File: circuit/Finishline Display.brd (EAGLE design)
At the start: 81.3 x 100 mm, 25 parts, among them U1 PCA9501, U2 HEF4066BT, U3 TM1637

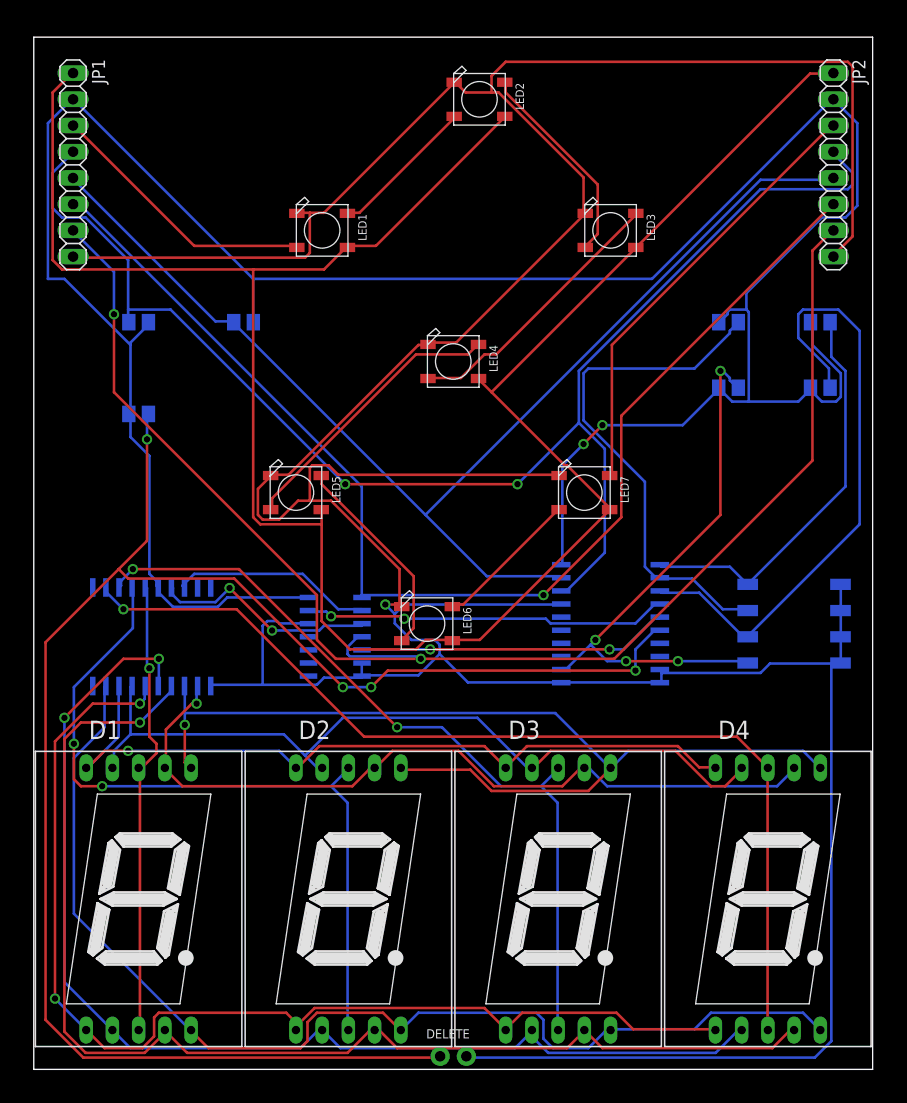
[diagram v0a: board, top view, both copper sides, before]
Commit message: changes circuit to include capacitors
This change adds resistors and capacitors to the LED driver chip
as well as individual caps to each WS2812 LED.
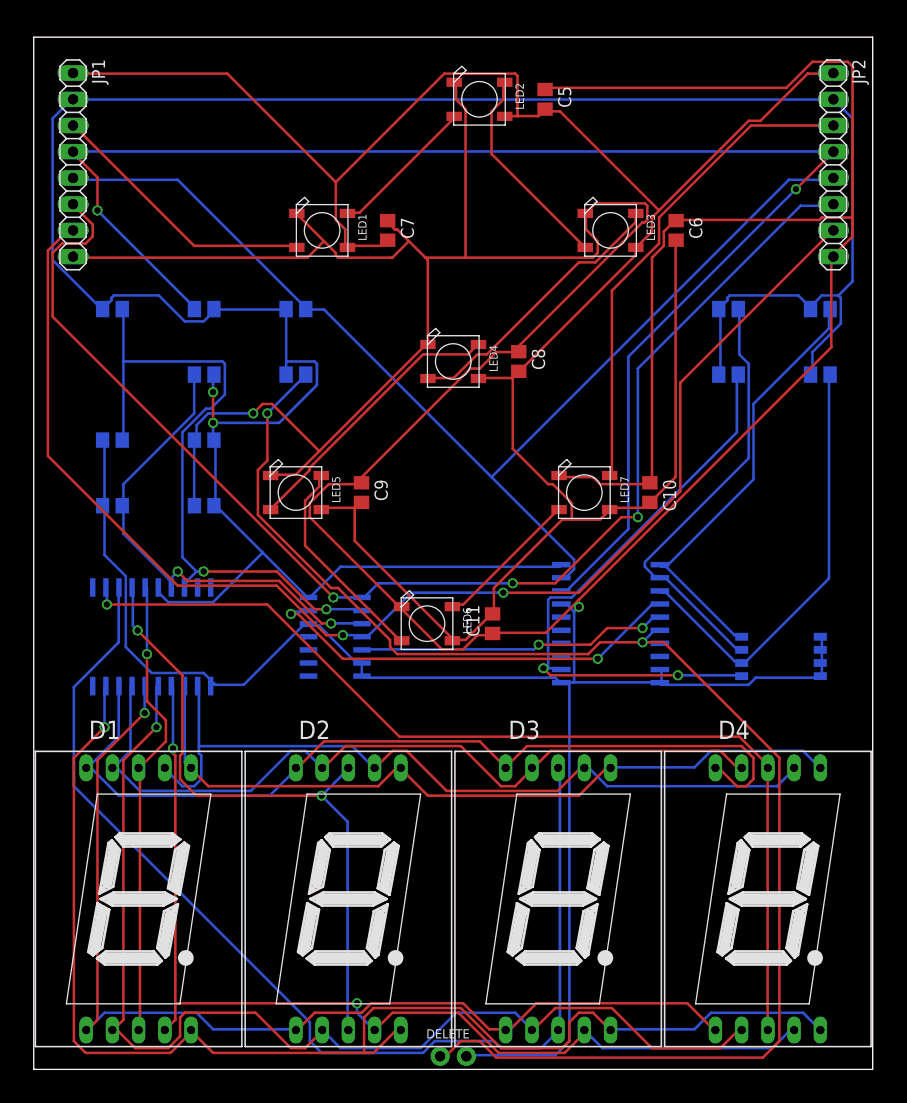
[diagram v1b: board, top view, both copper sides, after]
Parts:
- removed S1: SWS004, smd-special:SMS-004
- added C1, C2: 1nF, rcl:C0805
- added C10, C11, C4, C5, C6, C7, C8, C9: 100nF, rcl:C0805
- added C3: 10nF, rcl:C0805
- added R10, R9: 10K, resistor:M0805
- added SW1: 416131160804, Wurth_Elektronik_Electromechanic_Switchs_rev15b:416131160804
- moved R7 15.7 mm to (25.4, 67.3)
- moved R5 6.48 mm to (16.5, 73.7)
- moved R6 5.24 mm to (25.4, 73.7), turned to 180 degrees
- moved R1 1.27 mm to (76.2, 73.7)
- moved R2 1.27 mm to (67.3, 73.7)
- moved R3 1.27 mm to (76.2, 67.3)
- moved R4 1.27 mm to (67.3, 67.3)
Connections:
- net +5V: now also C10.2, C11.2, C5.2, C6.2, C7.2, C8.2, C9.2
- net 0V: now also C1.1, C10.1, C11.1, C2.1, C3.2, C4.2, C5.1, C6.1, C7.1, C8.1, C9.1, SW1.1, SW1.2, SW1.3, SW1.4; no longer S1.1, S1.2, S1.3, S1.4
- net 3.3V: now also C3.1, C4.1, R10.2, R9.2
- net N$14: now also SW1.8; no longer S1.8
- net N$15: now also SW1.7; no longer S1.7
- net N$16: now also SW1.6; no longer S1.6
- net N$17: now also SW1.5; no longer S1.5
- net N$18: now also C1.2, R9.1
- net N$19: now also C2.2, R10.1
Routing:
- net 0V: track 402.7 -> 526.9 mm, vias 1 -> 2
- net N$18: track 19.7 -> 65.3 mm, vias 0 -> 2
- net N$11: track 77.4 -> 106.9 mm, vias 2 -> 0
- net N$19: track 22.1 -> 46.6 mm
- net N$20: track 163.3 -> 141.5 mm, vias 4 -> 2
- net SEG2: track 95.6 -> 74.4 mm, vias 1 -> 0
- net SEG3: track 118.5 -> 100.5 mm, vias 1 -> 2
- net N$16: track 59.9 -> 42.5 mm
- net SEG8: track 109.5 -> 124.8 mm, vias 0 -> 1
- net +5V: track 209.8 -> 224.9 mm
- net SEG7: track 75.1 -> 86.6 mm, vias 1 -> 0
- net N$10: track 72.9 -> 62.6 mm
- net SCL: track 137.2 -> 147.5 mm
- net DIO: track 139.1 -> 129.0 mm
- net CLK: track 117.5 -> 125.7 mm, vias 1 -> 3
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
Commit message: add Controller brd+sch, fix Display LDR line
An additional board for the controller was added as a Due shield.
The LDR was hooked up to a digital pin, has been changed to use
a separate line which gets patched through the 4066.
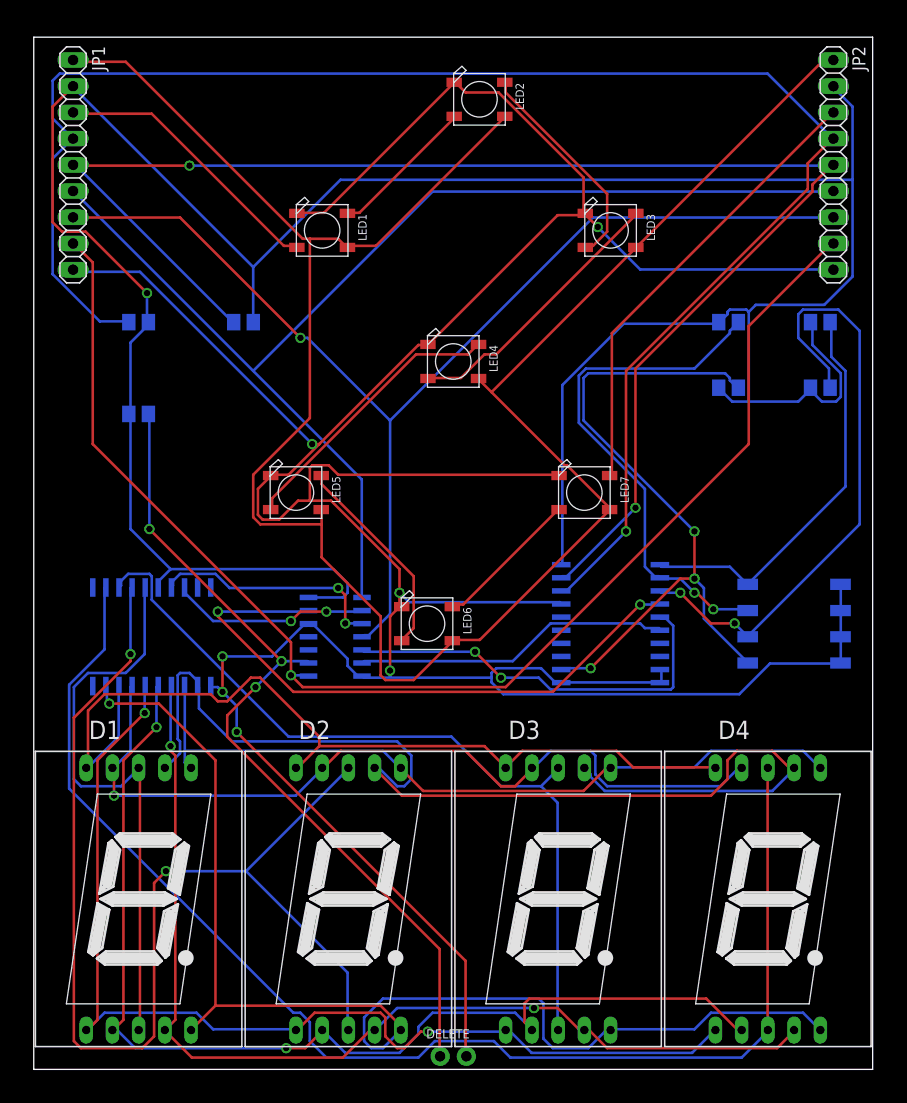
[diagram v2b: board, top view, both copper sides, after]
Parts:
- removed C1, C2: 1nF, rcl:C0805
- removed C10, C11, C4, C5, C6, C7, C8, C9: 100nF, rcl:C0805
- removed C3: 10nF, rcl:C0805
- removed R10, R9: 10K, resistor:M0805
- removed SW1: 416131160804, Wurth_Elektronik_Electromechanic_Switchs_rev15b:416131160804
- added S1: SWS004, smd-special:SMS-004
- JP1, JP2: device pinhead:1X08 -> pinhead:1X09
- moved R7 15.7 mm to (10.2, 63.5)
- moved R5 6.48 mm to (10.2, 72.4)
- moved R6 5.24 mm to (20.3, 72.4), turned to 0 degrees
- moved R1 1.27 mm to (76.2, 72.4)
- moved R2 1.27 mm to (67.3, 72.4)
- moved R3 1.27 mm to (76.2, 66.0)
- moved R4 1.27 mm to (67.3, 66.0)
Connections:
- removed net 0V: C1.1, C10.1, C11.1, C2.1, C3.2, C4.2, C5.1, C6.1, C7.1, C8.1, C9.1, JP1.8, JP2.8, LED1.3-GND, LED2.3-GND, LED3.3-GND, LED4.3-GND, LED5.3-GND, LED6.3-GND, LED7.3-GND, R8.2, SW1.1, SW1.2, SW1.3, SW1.4, U1.10, U1.11, U1.17, U1.9, U2.12, U2.6, U2.7, U3.1
- new net GND: JP1.9, JP2.9, LED1.3-GND, LED2.3-GND, LED3.3-GND, LED4.3-GND, LED5.3-GND, LED6.3-GND, LED7.3-GND, R8.2, S1.1, S1.2, S1.3, S1.4, U1.10, U1.11, U1.17, U1.9, U2.12, U2.7, U3.1
- new net LDR: JP1.8, JP2.8, U2.8
- new net N$23: U1.6, U2.6
- net +5V: no longer C10.2, C11.2, C5.2, C6.2, C7.2, C8.2, C9.2
- net 3.3V: no longer C3.1, C4.1, R10.2, R9.2
- net N$14: now also S1.8; no longer SW1.8
- net N$15: now also S1.7; no longer SW1.7
- net N$16: now also S1.6; no longer SW1.6
- net N$17: now also S1.5; no longer SW1.5
- net N$18: no longer C1.2, R9.1
- net N$19: no longer C2.2, R10.1
- net N$20: now also U2.9; no longer U1.6
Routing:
- net 0V: track 526.9 -> 0.00 mm, vias 2 -> 0
- net GND: track 0.00 -> 358.2 mm, vias 0 -> 7
- net LDR: track 0.00 -> 129.9 mm, vias 0 -> 1
- net N$20: track 141.5 -> 81.0 mm, vias 2 -> 3
- net N$10: track 62.6 -> 112.7 mm
- net N$18: track 65.3 -> 19.3 mm
- net SDA: track 111.6 -> 147.0 mm, vias 0 -> 2
- net SEG1: track 77.1 -> 111.8 mm
- net N$23: track 0.00 -> 30.8 mm
- net N$12: track 98.1 -> 128.4 mm, vias 1 -> 0
- net N$11: track 106.9 -> 78.3 mm
- net N$19: track 46.6 -> 22.9 mm
- net +5V: track 224.9 -> 203.1 mm
- net 3.3V: track 253.9 -> 272.3 mm, vias 2 -> 1
- net N$16: track 42.5 -> 59.9 mm, vias 0 -> 2
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
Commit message: add mounting holes to the Finishline Display board
New PDFs have been added for the display.
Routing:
- net 3.3V: track 272.3 -> 218.0 mm, vias 1 -> 4
- net N$10: track 112.7 -> 68.9 mm
- net SEG1: track 111.8 -> 77.8 mm, vias 0 -> 3
- net N$12: track 128.4 -> 98.3 mm, vias 0 -> 1
- net N$17: track 66.6 -> 90.0 mm, vias 3 -> 5
- net SCL: track 163.3 -> 178.9 mm
- net N$1: track 58.7 -> 44.5 mm
- net N$9: track 56.4 -> 43.5 mm, vias 0 -> 2
- net LDR: track 129.9 -> 142.5 mm
- net N$15: track 50.6 -> 39.2 mm, vias 2 -> 0
- net SEG7: track 86.3 -> 76.3 mm
- net N$13: track 39.4 -> 30.2 mm, vias 2 -> 0
- net +5V: track 203.1 -> 196.6 mm, vias 0 -> 2
- net DIO: track 112.3 -> 118.6 mm, vias 1 -> 3
- net CLK: track 114.4 -> 108.5 mm
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
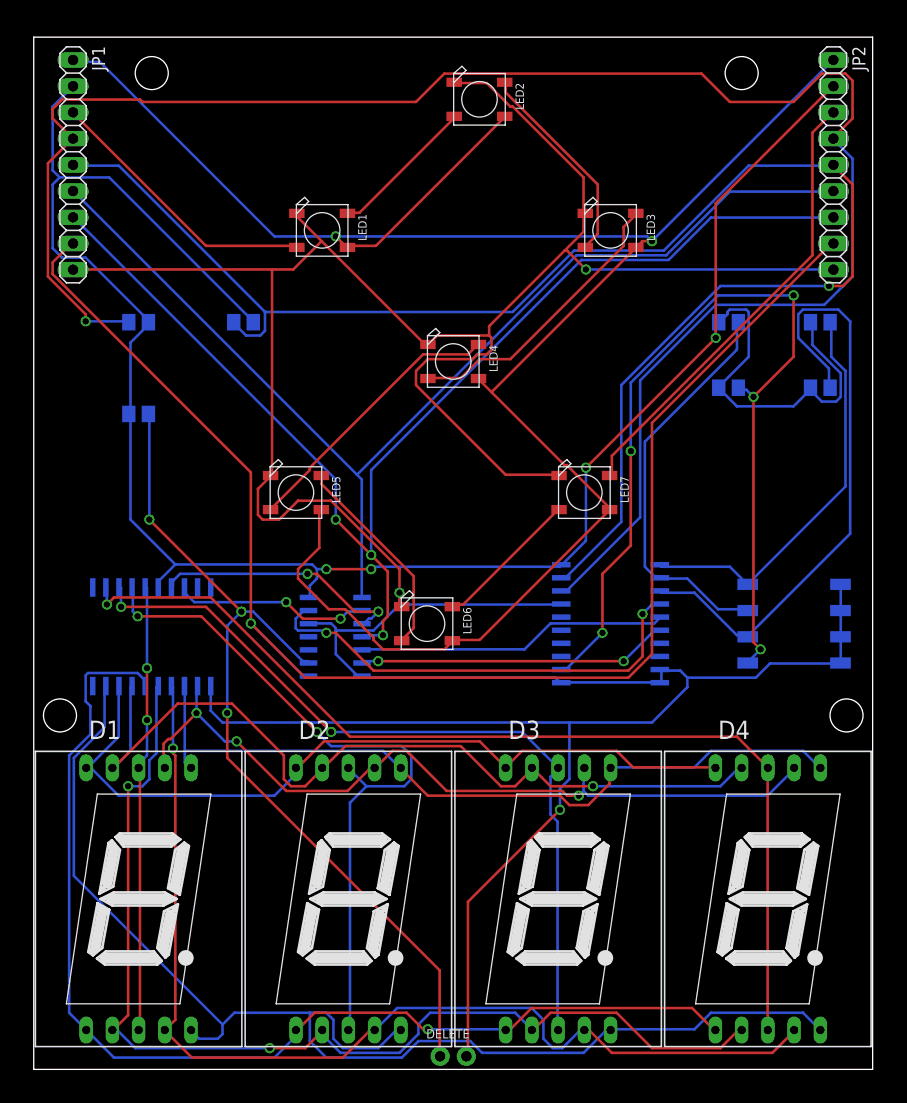
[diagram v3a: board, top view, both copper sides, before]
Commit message: finalize display module and controller shield
Display Module: Reordered the WS2813 LEDs to be consistent with normal
7-segment LED numbers (a-g). Changed schematics to be in the same
orientation as the board in top view. Re-adds the capacitors for the
WS2812 LEDs and the LDR line, which inadvertently got lost in the last
commit. Added silk screen.

Controller Shield: Added large electrolyte capacitor to buffer for the
WS2812 LEDs. Added a series resistor for the WS2812 data line. Added
silk screen and corrected wrong pinout of the I2C and serial header.
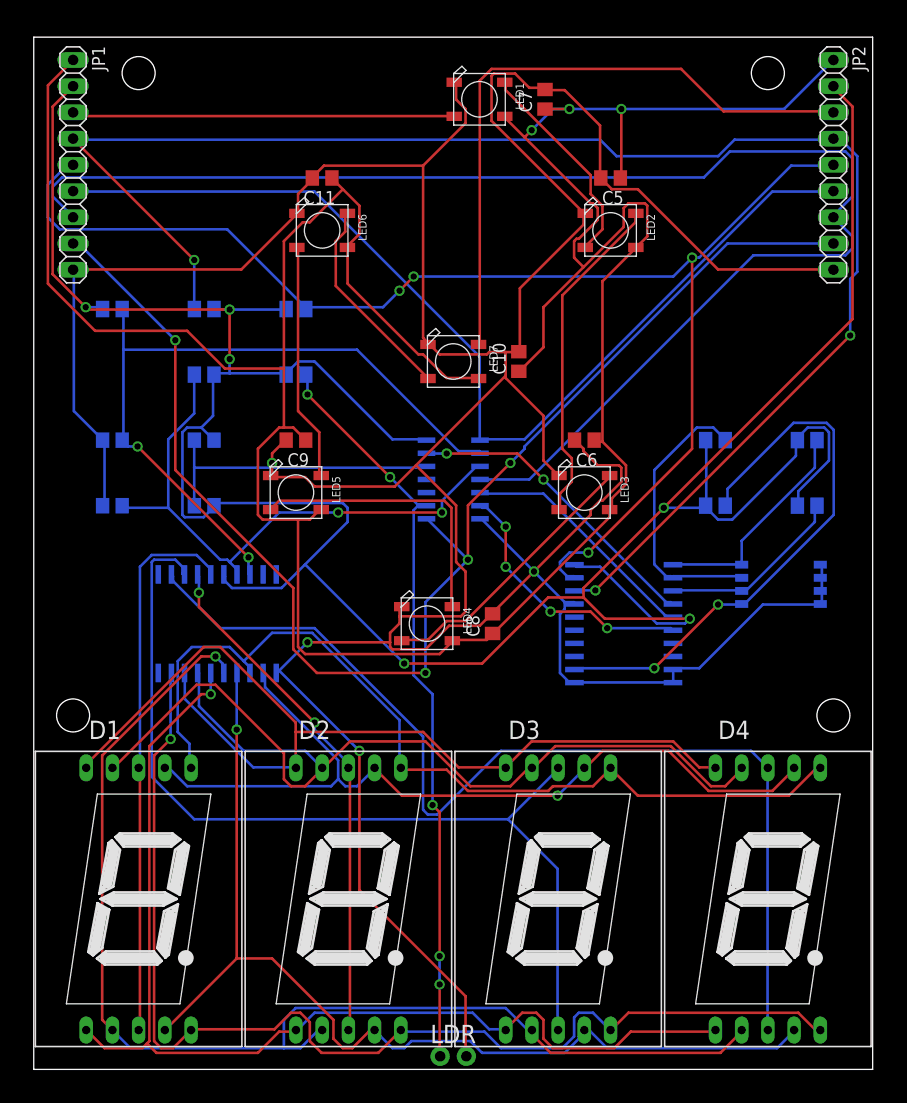
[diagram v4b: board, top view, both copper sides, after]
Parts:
- removed S1: SWS004, smd-special:SMS-004
- added C1, C2: 1nF, rcl:C0805
- added C10, C11, C4, C5, C6, C7, C8, C9: 100nF, rcl:C0805
- added C3: 10nF, rcl:C0805
- added R10, R9: 10K, resistor:M0805
- added SW1: (no value), Wurth_Elektronik_Electromechanic_Switchs_rev15b:416131160804
- moved LED6 39.4 mm to (27.9, 81.3)
- moved LED3 25.5 mm to (53.3, 55.9)
- moved LED4 25.5 mm to (38.1, 43.2)
- moved LED1 19.8 mm to (43.2, 94.0)
- moved U2 19.1 mm to (40.6, 57.1)
- moved LED2 18.0 mm to (55.9, 81.3)
- moved LED7 18.0 mm to (40.6, 68.6)
- moved R7 15.7 mm to (25.4, 67.3)
- moved R3 11.5 mm to (74.9, 54.6)
- moved R4 11.5 mm to (66.0, 54.6)
- moved R1 11.5 mm to (74.9, 61.0)
- moved R2 11.5 mm to (66.0, 61.0)
- moved U3 6.48 mm to (17.8, 43.2)
- moved R5 6.48 mm to (16.5, 73.7)
- moved R6 5.24 mm to (25.4, 73.7), turned to 180 degrees
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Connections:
- removed net 3.3V: JP1.2, JP2.2, R1.2, R2.2, R3.2, R4.2, R5.1, R6.1, R7.2, U1.20, U2.14, U3.16
- new net +3V3: C3.1, C4.1, JP1.2, JP2.2, R1.2, R10.2, R2.2, R3.2, R4.2, R5.1, R6.1, R7.2, R9.2, U1.20, U2.14, U3.16
- net +5V: now also C10.1, C11.1, C5.1, C6.1, C7.1, C8.1, C9.1
- net GND: now also C1.1, C10.2, C11.2, C2.1, C3.2, C4.2, C5.2, C6.2, C7.2, C8.2, C9.2, SW1.1, SW1.2, SW1.3, SW1.4; no longer S1.1, S1.2, S1.3, S1.4
- net N$14: now also SW1.8; no longer S1.8
- net N$15: now also SW1.7; no longer S1.7
- net N$16: now also SW1.6; no longer S1.6
- net N$17: now also SW1.5; no longer S1.5
- net N$18: now also C1.2, R9.1
- net N$19: now also C2.2, R10.1
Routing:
- net +3V3: track 0.00 -> 284.2 mm, vias 0 -> 6
- net 3.3V: track 218.0 -> 0.00 mm, vias 4 -> 0
- net +5V: track 196.6 -> 289.6 mm, vias 2 -> 3
- net GND: track 363.3 -> 427.6 mm, vias 3 -> 4
- net N$18: track 19.1 -> 70.3 mm
- net N$16: track 59.1 -> 18.2 mm
- net N$17: track 90.0 -> 54.7 mm, vias 5 -> 2
- net N$19: track 24.4 -> 56.9 mm
- net SCL: track 178.9 -> 154.1 mm, vias 1 -> 3
- net SDA: track 150.7 -> 130.4 mm, vias 1 -> 4
- net DIO: track 118.6 -> 138.5 mm, vias 3 -> 0
- net N$10: track 68.9 -> 50.3 mm
- net N$8: track 44.3 -> 62.1 mm
- net N$14: track 39.2 -> 21.8 mm
- net SEG7: track 76.3 -> 93.1 mm
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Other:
- board text added: "(c) 2018 MICHAEL ROMMEL"
- board text added: "I2C ADDRESS SELECT"
- board text added: "LDR"
- board text added: "PINEWOOD DERBY FINISHLINE DISPLAY MODULE"

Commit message: create the final schematics and boards
Some schematics errors have been corrected. Another connector for
the laser diodes of the Finishing Gate has been added. The
connectors to the daughterboards have been rotated, so that the
cabling will run mostly straight.

All gerber files have been added as well as .zip files for the
boardhouse.
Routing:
- net GND: vias 4 -> 20
- added copper zone on layer 1, net GND
- added copper zone on layer 16, net GND
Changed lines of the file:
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@@
 <via x="48.4632" y="48.2346" extent="1-16" drill="0.6096"/>
 <via x="23.0886" y="58.7502" extent="1-16" drill="0.6096"/>
+<polygon width="0.4064" layer="16">
+<vertex x="-1.27" y="101.6"/>
+<vertex x="82.55" y="101.6"/>
+<vertex x="82.55" y="-1.27"/>
+<vertex x="-1.27" y="-1.27"/>
+</polygon>
+<polygon width="0.4064" layer="1">
+<vertex x="-1.27" y="101.6"/>
+<vertex x="82.55" y="101.6"/>
+<vertex x="82.55" y="-1.27"/>
+<vertex x="-1.27" y="-1.27"/>
+</polygon>
+<via x="21.59" y="64.77" extent="1-16" drill="0.6"/>
+<via x="22.86" y="20.32" extent="1-16" drill="0.6"/>
+<via x="20.32" y="6.35" extent="1-16" drill="0.6"/>
+<via x="8.89" y="8.89" extent="1-16" drill="0.6"/>
+<via x="36.83" y="83.82" extent="1-16" drill="0.6"/>
+<via x="17.78" y="95.25" extent="1-16" drill="0.6"/>
+<via x="46.99" y="74.93" extent="1-16" drill="0.6"/>
+<via x="21.59" y="82.55" extent="1-16" drill="0.6"/>
+<via x="20.32" y="77.47" extent="1-16" drill="0.6"/>
+<via x="21.59" y="44.45" extent="1-16" drill="0.6"/>
+<via x="13.97" y="43.18" extent="1-16" drill="0.6"/>
+<via x="24.13" y="50.8" extent="1-16" drill="0.6"/>
+<via x="66.04" y="50.8" extent="1-16" drill="0.6"/>
+<via x="73.66" y="82.55" extent="1-16" drill="0.6"/>
+<via x="33.02" y="64.77" extent="1-16" drill="0.6"/>
+<via x="60.96" y="12.7" extent="1-16" drill="0.6"/>
 </signal>
 <signal name="LDR">
